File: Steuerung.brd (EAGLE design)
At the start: 114.3 x 48.9 mm, 15 parts

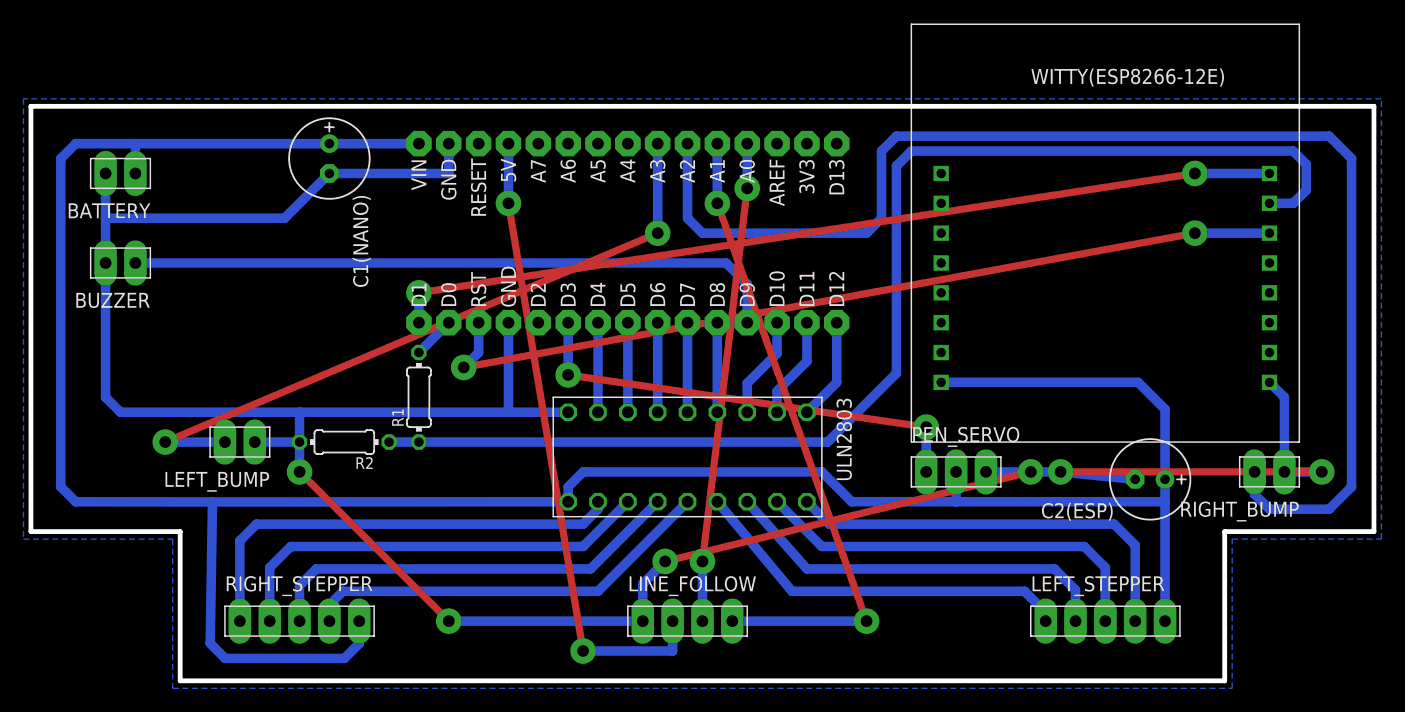
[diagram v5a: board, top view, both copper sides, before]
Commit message: PCB Resize
Made the PCB even smaller to be millable on the Proxxon MF 70.
This is the Version currently being tested in the Lab.
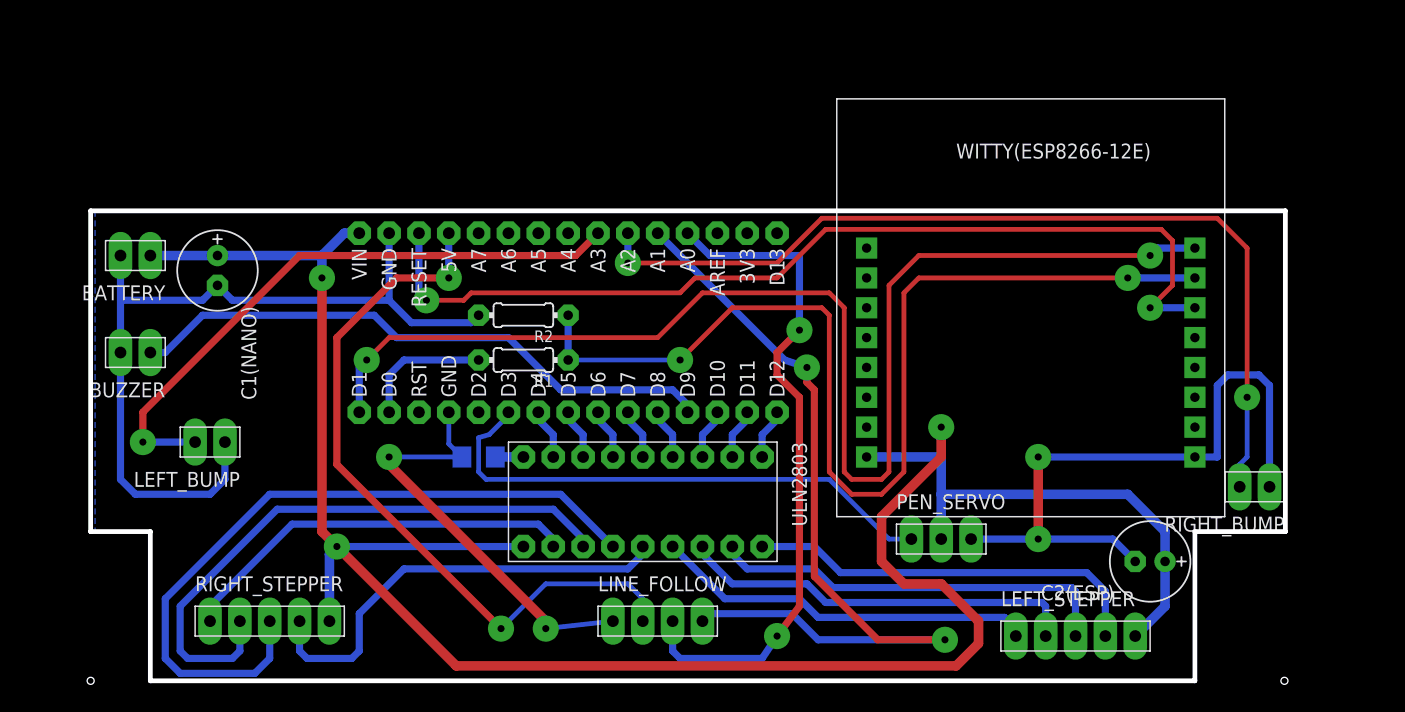
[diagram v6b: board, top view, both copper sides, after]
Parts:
- added R4: 0, rcl-2:R1206
- WITTY(ESP8266-12E): value ESP -> ESPWITTY
- moved R2 18.7 mm to (36.8, 31.1)
- moved C1(NANO) 13.5 mm to (10.8, 34.9)
- moved R1 9.44 mm to (36.8, 27.3), turned to 180 degrees
- moved ARDUINO_NANO 9.16 mm to (40.6, 30.5)
- moved WITTY(ESP8266-12E) 8.98 mm to (66.0, 36.8)
- moved BUZZER 7.73 mm to (3.81, 27.9)
- moved BATTERY 7.10 mm to (3.81, 36.2)
- moved C2(ESP) 6.98 mm to (90.2, 10.2)
- moved PEN_SERVO 5.85 mm to (72.4, 12.1)
- moved ULN2803 5.39 mm to (47.0, 15.2)
- moved LEFT_STEPPER 2.84 mm to (83.8, 3.81)
- moved RIGHT_STEPPER 2.54 mm to (15.2, 5.08)
- moved LEFT_BUMP 2.54 mm to (10.2, 20.3)
- moved LINE_FOLLOW 2.54 mm to (48.3, 5.08)
- moved RIGHT_BUMP 1.80 mm to (99.1, 16.5)
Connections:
- new net N$29: R4.2, ULN2803.P$9
- net GND: now also R4.1; no longer ULN2803.P$9
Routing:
- net GND: track 227.4 -> 163.7 mm, vias 6 -> 4
- net N$21: track 75.7 -> 109.8 mm
- net N$18: track 110.4 -> 78.5 mm, vias 0 -> 2
- net VSS: track 227.1 -> 197.9 mm, vias 0 -> 3
- net N$6: track 36.5 -> 61.8 mm
- net N$26: track 40.9 -> 57.6 mm
- net N$25: track 54.3 -> 70.9 mm
- net N$20: track 104.9 -> 89.9 mm, vias 0 -> 2
- net N$7: track 37.4 -> 51.4 mm
- net N$22: track 74.0 -> 82.7 mm
- net N$30: track 53.9 -> 62.1 mm
- net N$19: track 3.59 -> 11.3 mm
- net N$24: track 39.1 -> 45.6 mm, vias 2 -> 0
- net N$28: track 58.2 -> 52.0 mm, vias 2 -> 1
- net N$23: track 56.1 -> 50.8 mm
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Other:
- board size 114.3 x 48.9 mm -> 101.7 x 40 mm
